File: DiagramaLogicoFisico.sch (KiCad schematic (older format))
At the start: 23 parts, among them J1 Conn_01x02, J2 Conn_01x03, J3 Conn_01x03, J4 Conn_01x04, J5 Conn_01x05, U1 TC1262-33, U2 DSPIC33EP128GM604, Y1 7Mhz

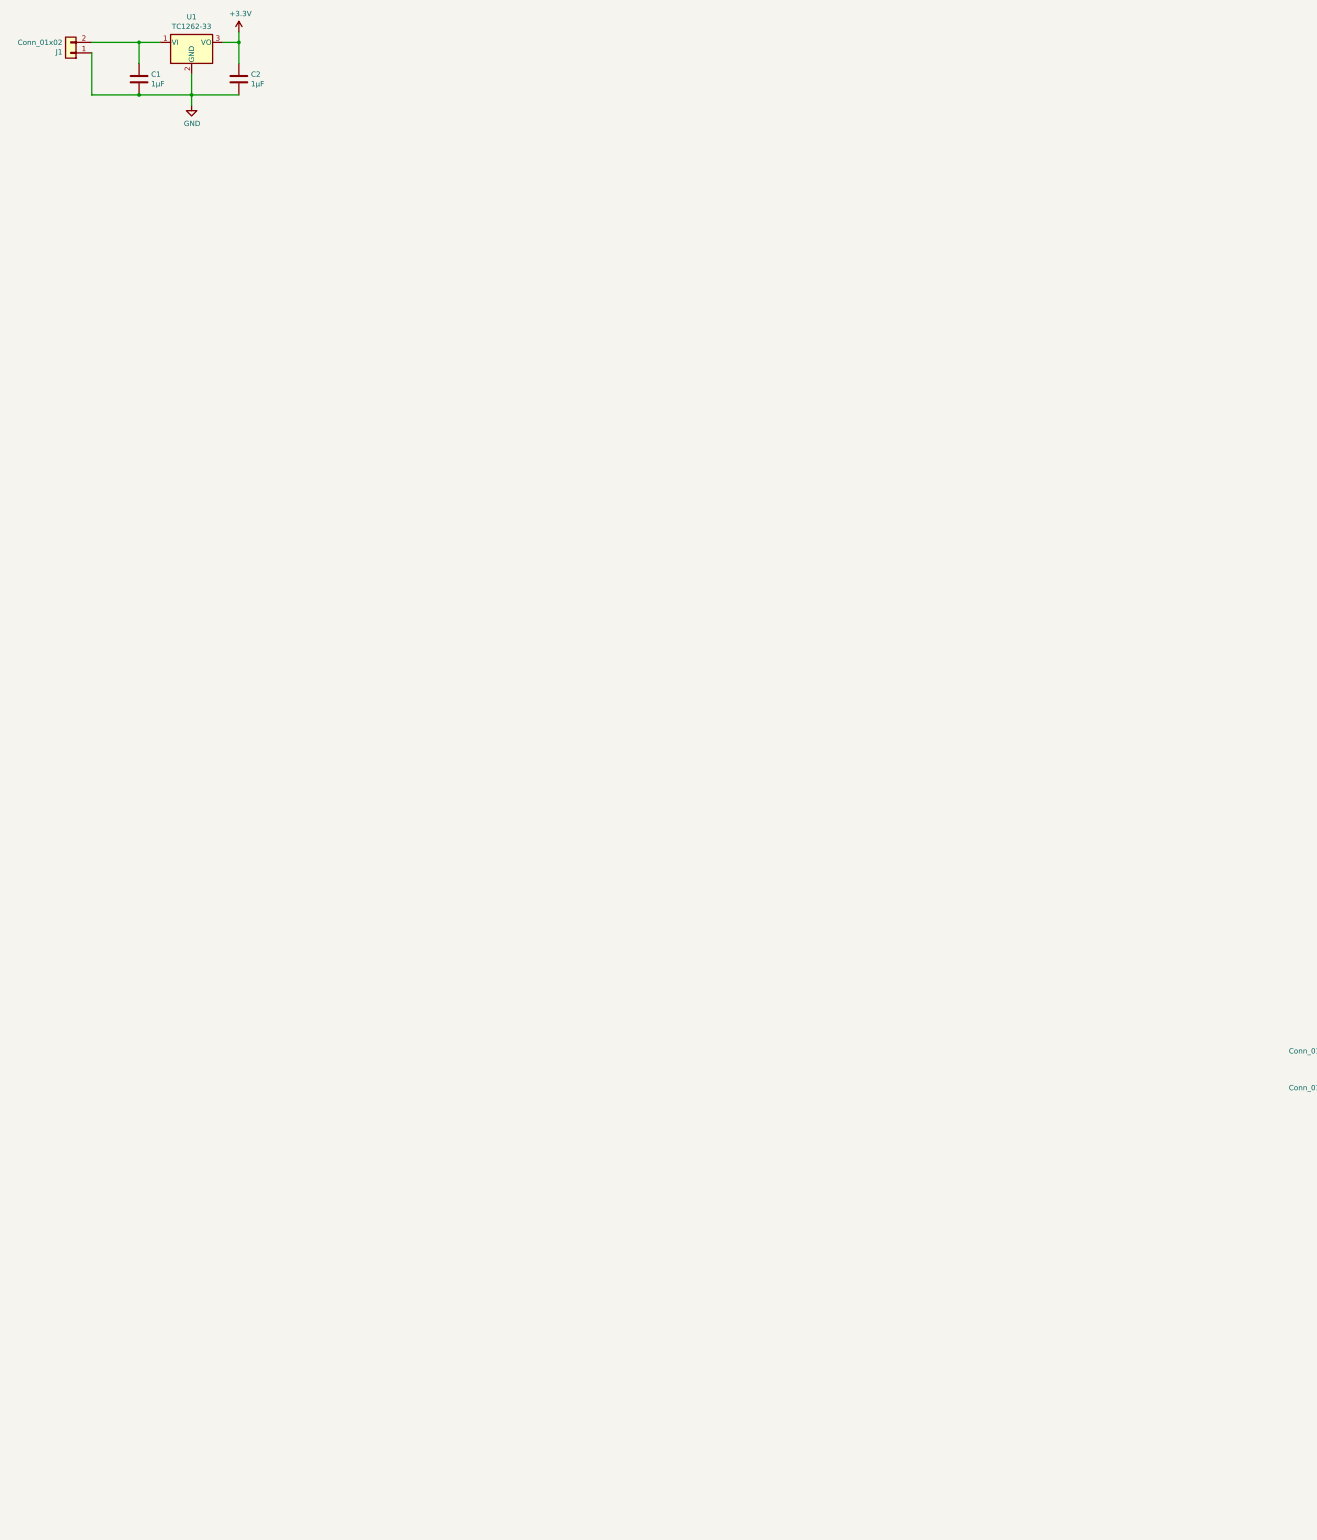
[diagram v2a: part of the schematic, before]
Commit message: Añadido el circuito de alimentación de motores y MCU, en principio se ha terminado el circuito lógico
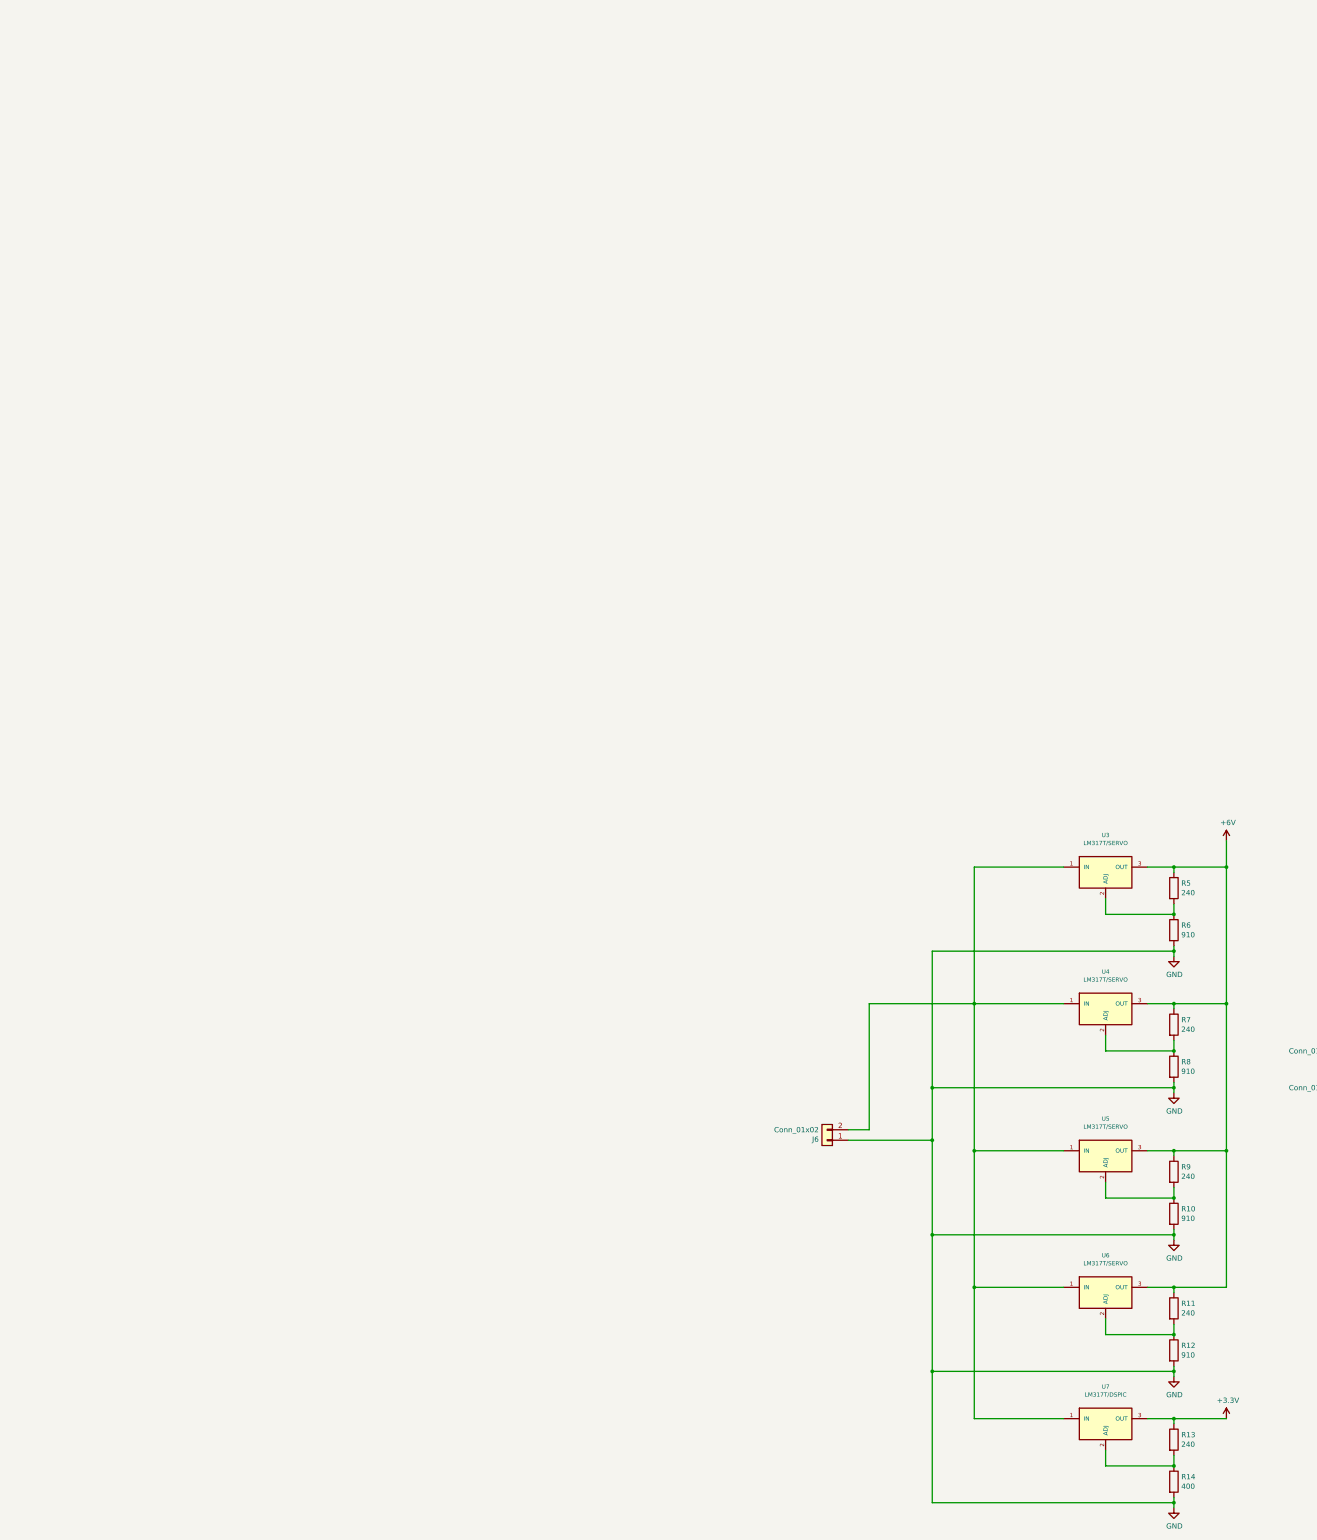
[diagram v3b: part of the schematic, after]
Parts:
- removed C1, C2: 1µF, symbol Device:C
- removed J1: Conn_01x02, TerminalBlock:TerminalBlock_bornier-2_P5.08mm, symbol Connector_Generic:Conn_01x02
- removed U1: TC1262-33, symbol Regulator_Linear:TC1262-33
- added J6: Conn_01x02, TerminalBlock:TerminalBlock_bornier-2_P5.08mm, symbol Connector_Generic:Conn_01x02
- added R10, R12, R6, R8: 910, Resistor_THT:R_Axial_DIN0204_L3.6mm_D1.6mm_P5.08mm_Horizontal, symbol Device:R
- added R11, R13, R5, R7, R9: 240, Resistor_THT:R_Axial_DIN0204_L3.6mm_D1.6mm_P5.08mm_Horizontal, symbol Device:R
- added R14: 400, Resistor_THT:R_Axial_DIN0204_L3.6mm_D1.6mm_P5.08mm_Horizontal, symbol Device:R
- added U3, U4, U5, U6: LM317T/SERVO, Package_TO_SOT_THT:TO-220-3_Vertical, symbol NCP:LM317T
- added U7: LM317T/DSPIC, Package_TO_SOT_THT:TO-220-3_Vertical, symbol NCP:LM317T
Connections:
- net +3V3: now also R13.1, U7.3 (OUT)
- net GND: now also J6.1 (Pin_1), R10.2, R12.2, R14.2, R6.2, R8.2
- new net: J6.2 (Pin_2), U3.1 (IN), U4.1 (IN), U5.1 (IN), U6.1 (IN), U7.1 (IN)
- new net: R5.2, R6.1, U3.2 (ADJ)
- new net: R7.2, R8.1, U4.2 (ADJ)
- new net: R10.1, R9.2, U5.2 (ADJ)
- new net: R11.2, R12.1, U6.2 (ADJ)
- new net: R13.2, R14.1, U7.2 (ADJ)
- new net +6V: R11.1, R5.1, R7.1, R9.1, U3.3 (OUT), U4.3 (OUT), U5.3 (OUT), U6.3 (OUT)

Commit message: Arreglados diversos errores tras la revisión de Norberto y finalizado el circuito lógico
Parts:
- removed C5TANTALUM1: 10µF, Capacitor_THT:C_Disc_D3.8mm_W2.6mm_P2.50mm, symbol Device:C
- added C1: Tantalo 10uF, symbol Device:CP1
- added J1, J7, J8, J9: Conn_01x02, TerminalBlock:TerminalBlock_bornier-2_P5.08mm, symbol Connector_Generic:Conn_01x02
- added R15: 1M, Resistor_THT:R_Axial_DIN0204_L3.6mm_D1.6mm_P5.08mm_Horizontal, symbol Device:R
- Y1: value 7Mhz -> 7.3728Mhz
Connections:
- net +3V3: now also J5.2 (Pin_2); no longer J5.5 (Pin_5)
- net GND: now also J5.3 (Pin_3), C1.2, J1.1 (Pin_1), J7.1 (Pin_1), J8.1 (Pin_1), J9.1 (Pin_1); no longer J5.4 (Pin_4)
- net at J5.1 (Pin_1): now also R4.2, U2.18 (MCLR); no longer U2.24 (RB3)
- net at U2.23 (RB2): now also J5.5 (Pin_5); no longer J5.2 (Pin_2)
- net at C4.2, U2.30 (RA2), Y1.1: now also R15.2
- net at C3.2, U2.31 (RA3), Y1.2: now also R15.1
- net at U2.7 (Vcap): now also C1.1
- removed net +6V: R11.1, R5.1, R7.1, R9.1, U3.3 (OUT), U4.3 (OUT), U5.3 (OUT), U6.3 (OUT)
- new net: J5.4 (Pin_4), U2.24 (RB3)
- new net: J1.2 (Pin_2), R5.1, U3.3 (OUT)
- new net: J7.2 (Pin_2), R7.1, U4.3 (OUT)
- new net: J8.2 (Pin_2), R9.1, U5.3 (OUT)
- new net: J9.2 (Pin_2), R11.1, U6.3 (OUT)
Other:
- moved on the sheet: J6, R10, R11, R12, R13, R14, R5, R6, R7, R8, R9, U3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

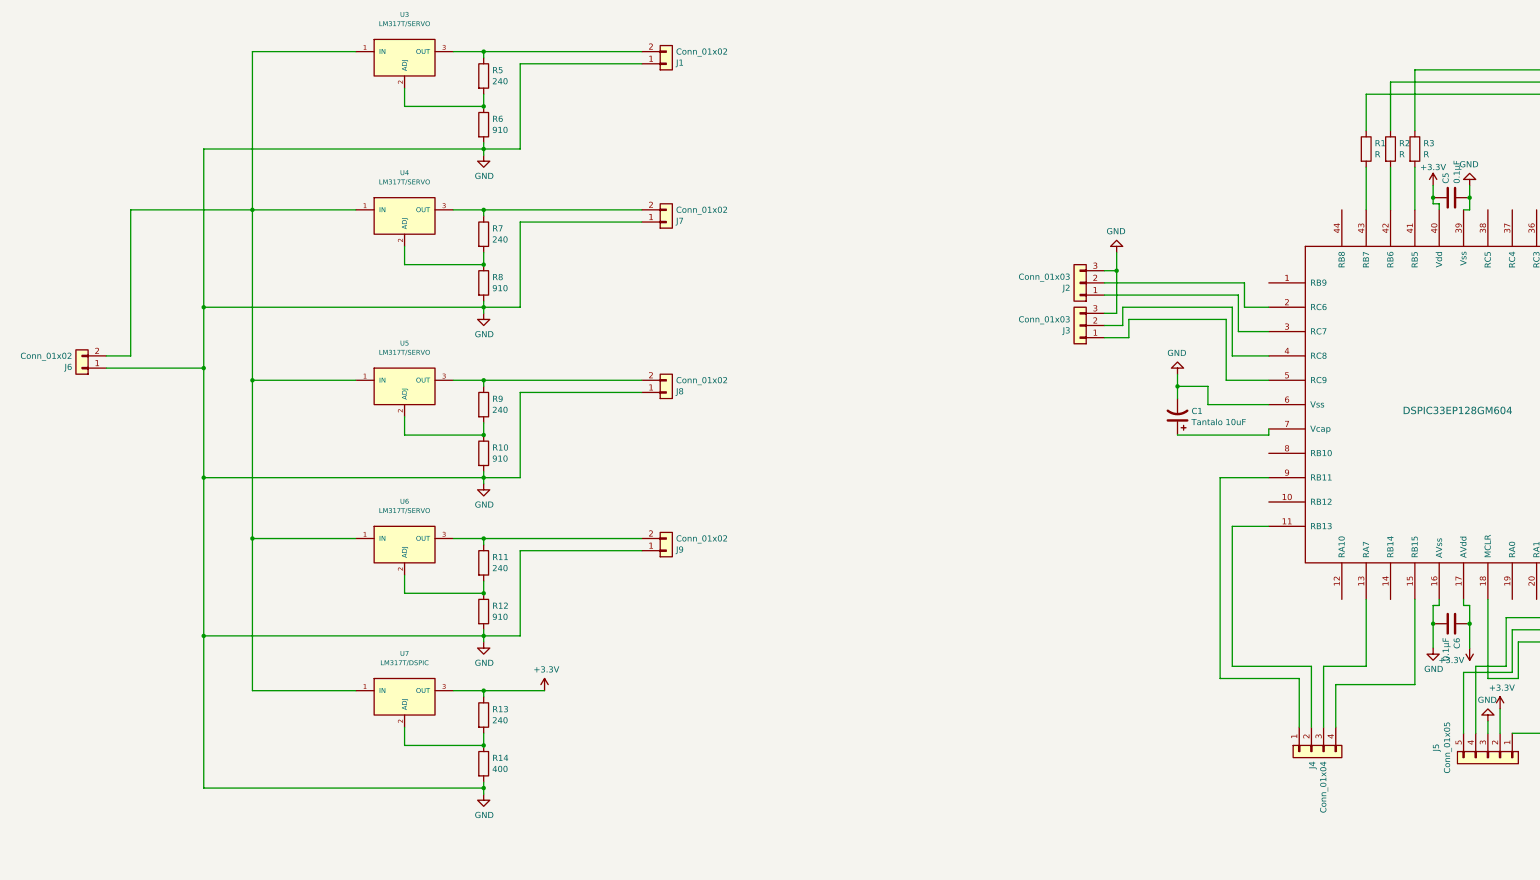
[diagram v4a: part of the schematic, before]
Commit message: Arreglados diversos errores tras la revisión de Norberto y finalizado el circuito lógico, añadidas etiquetas a cada componente
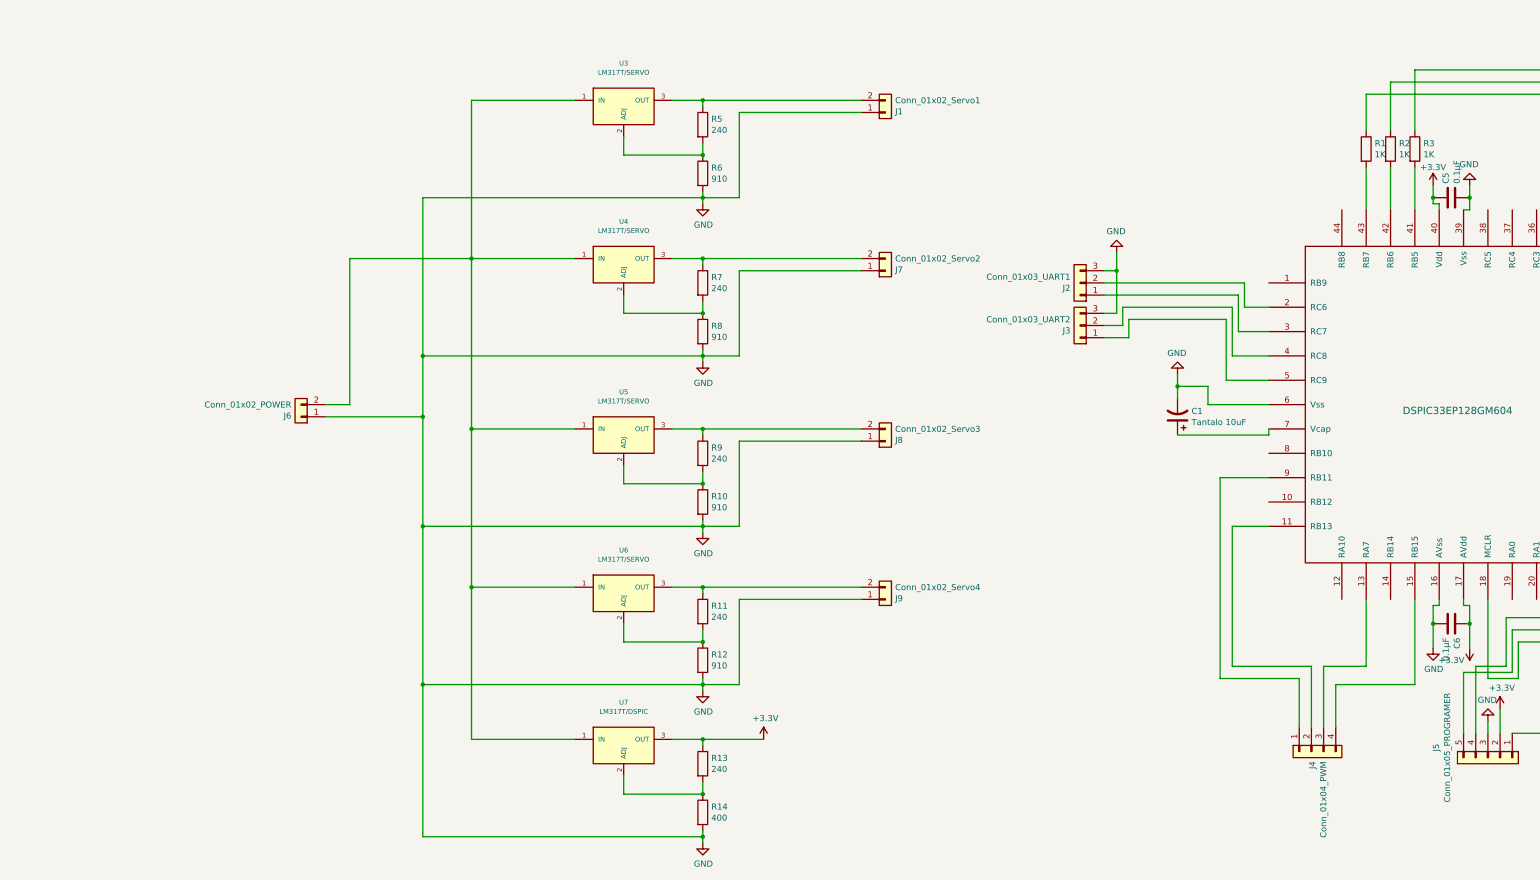
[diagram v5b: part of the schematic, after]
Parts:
- J1: value Conn_01x02 -> Conn_01x02_Servo1
- J2: value Conn_01x03 -> Conn_01x03_UART1
- J3: value Conn_01x03 -> Conn_01x03_UART2
- J4: value Conn_01x04 -> Conn_01x04_PWM
- J5: value Conn_01x05 -> Conn_01x05_PROGRAMER
- J6: value Conn_01x02 -> Conn_01x02_POWER
- J7: value Conn_01x02 -> Conn_01x02_Servo2
- J8: value Conn_01x02 -> Conn_01x02_Servo3
- J9: value Conn_01x02 -> Conn_01x02_Servo4
- R1, R2, R3: value R -> 1K
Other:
- moved on the sheet: J1, J6, J7, J8, J9, R10, R11, R12, R13, R14, R5, R6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

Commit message: Proyecto Almost Released
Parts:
- C1: footprint (none) -> Capacitor_THT:C_Disc_D3.8mm_W2.6mm_P2.50mm
- R1, R2, R3: value 1K -> K2
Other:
- moved on the sheet: J1, J6, J7, J8, J9, R10, R11, R12, R13, R14, R5, R6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

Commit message: Proyecto Almost finalizado
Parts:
- added J10: Conn_01x04_TRIS, Connector_PinHeader_2.54mm:PinHeader_1x04_P2.54mm_Vertical, symbol Connector_Generic:Conn_01x04
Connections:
- net at U2.19 (RA0): now also J10.1 (Pin_1)
- net at U2.20 (RA1): now also J10.2 (Pin_2)
- net at U2.21 (RB0): now also J10.3 (Pin_3)
- net at U2.22 (RB1): now also J10.4 (Pin_4)
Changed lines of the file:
@@
 Wire Wire Line
 	9650 13150 10650 13150
+Wire Wire Line
+	16900 13250 16900 13350
+Wire Wire Line
+	16900 13350 17550 13350
+Wire Wire Line
+	17550 13350 17550 13650
+Wire Wire Line
+	17550 13650 18700 13650
+Wire Wire Line
+	17100 13250 17100 13550
+Wire Wire Line
+	17300 13250 17300 13450
+Wire Wire Line
+	17300 13450 18700 13450
+Wire Wire Line
+	17500 13250 17900 13250
+Wire Wire Line
+	17900 13250 17900 13350
+Wire Wire Line
+	17900 13350 18700 13350
+$Comp
+L Connector_Generic:Conn_01x04 J10
+U 1 1 5EB8B1CB
+P 18900 13550
+F 0 "J10" H 18980 13542 50  0000 L CNN
+F 1 "Conn_01x04_TRIS" H 18980 13451 50  0000 L CNN
+F 2 "Connector_PinHeader_2.54mm:PinHeader_1x04_P2.54mm_Vertical" H 18900 13550 50  0001 C CNN
+F 3 "~" H 18900 13550 50  0001 C CNN
+	1    18900 13550
+	1    0    0    1
+$EndComp
+Wire Wire Line
+	17100 13550 18700 13550
 $EndSCHEMATC
